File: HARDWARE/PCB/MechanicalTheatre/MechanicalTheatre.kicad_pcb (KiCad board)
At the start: 2 copper layers, 142.5 x 185 mm, 171 parts, among them J1 Power In 5V/24V, J10 Conn_01x02_General Purpose 01, J11 RJ45 8x Socket, J12 RJ45 8x Socket, J13 Conn_01x02_General Purpose 05, J14 Conn_01x02_General Purpose 06, J15 Conn_01x02_General Purpose 07, J16 Conn_01x02_General Purpose 10, J17 Conn_01x02_General Purpose 09, J18 Conn_01x02_General Purpose 08, J19 Conn_01x02_General Purpose 11, J2 Conn_01x02_General Purpose 02, J20 Conn_01x02_General Purpose 12, J21 Conn_01x02_General Purpose 13, J22 Conn_01x02_General Purpose 14, J23 Conn_01x02_General Purpose 03, J3 Conn_01x02_General Purpose 04, J4 Conn_01x06_Relais, J5 PQG3FST112, J6 Conn_01x03_ExternalSensor, J8 Conn_01x04_I2C_Display_20x4, J9 Conn_01x03_ProximitySensor, U1 Teensy4.1_OuterPins, U10 SN74HC14S, U11 SN74AHCT125N, U12 SN74AHCT125N, U13 SN74AHCT125N, U14 SN74HC14S, U15 Teensy4.1_OuterPins, U16 LM1117-3.3, U2 ESP32-DEVKITC-32D, U3 SN74AHCT125N, U4 SN74AHCT125N, U5 SN74AHCT125N, U6 SN74HC14S, U7 SN74AHCT125N, U8 SN74AHCT125N, U9 SN74AHCT125N

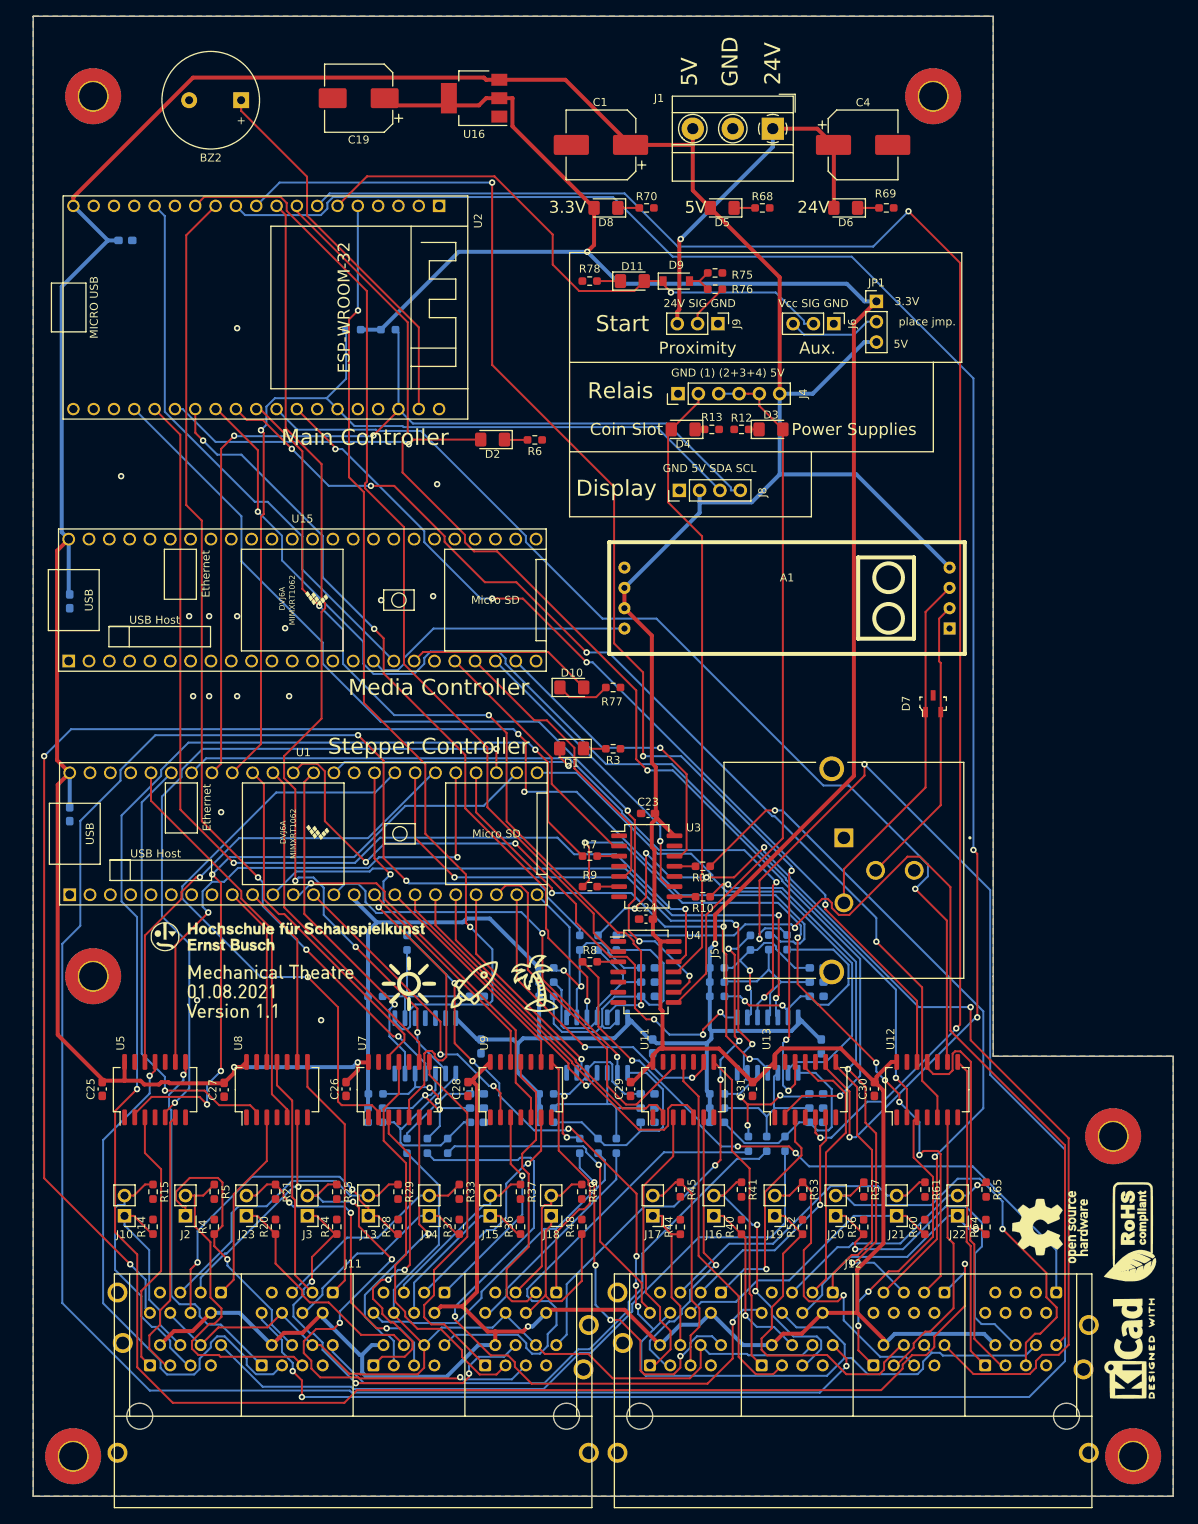
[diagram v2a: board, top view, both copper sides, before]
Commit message: pcb v1.2
- pcb v1.2 in production.
- startet to write a manual
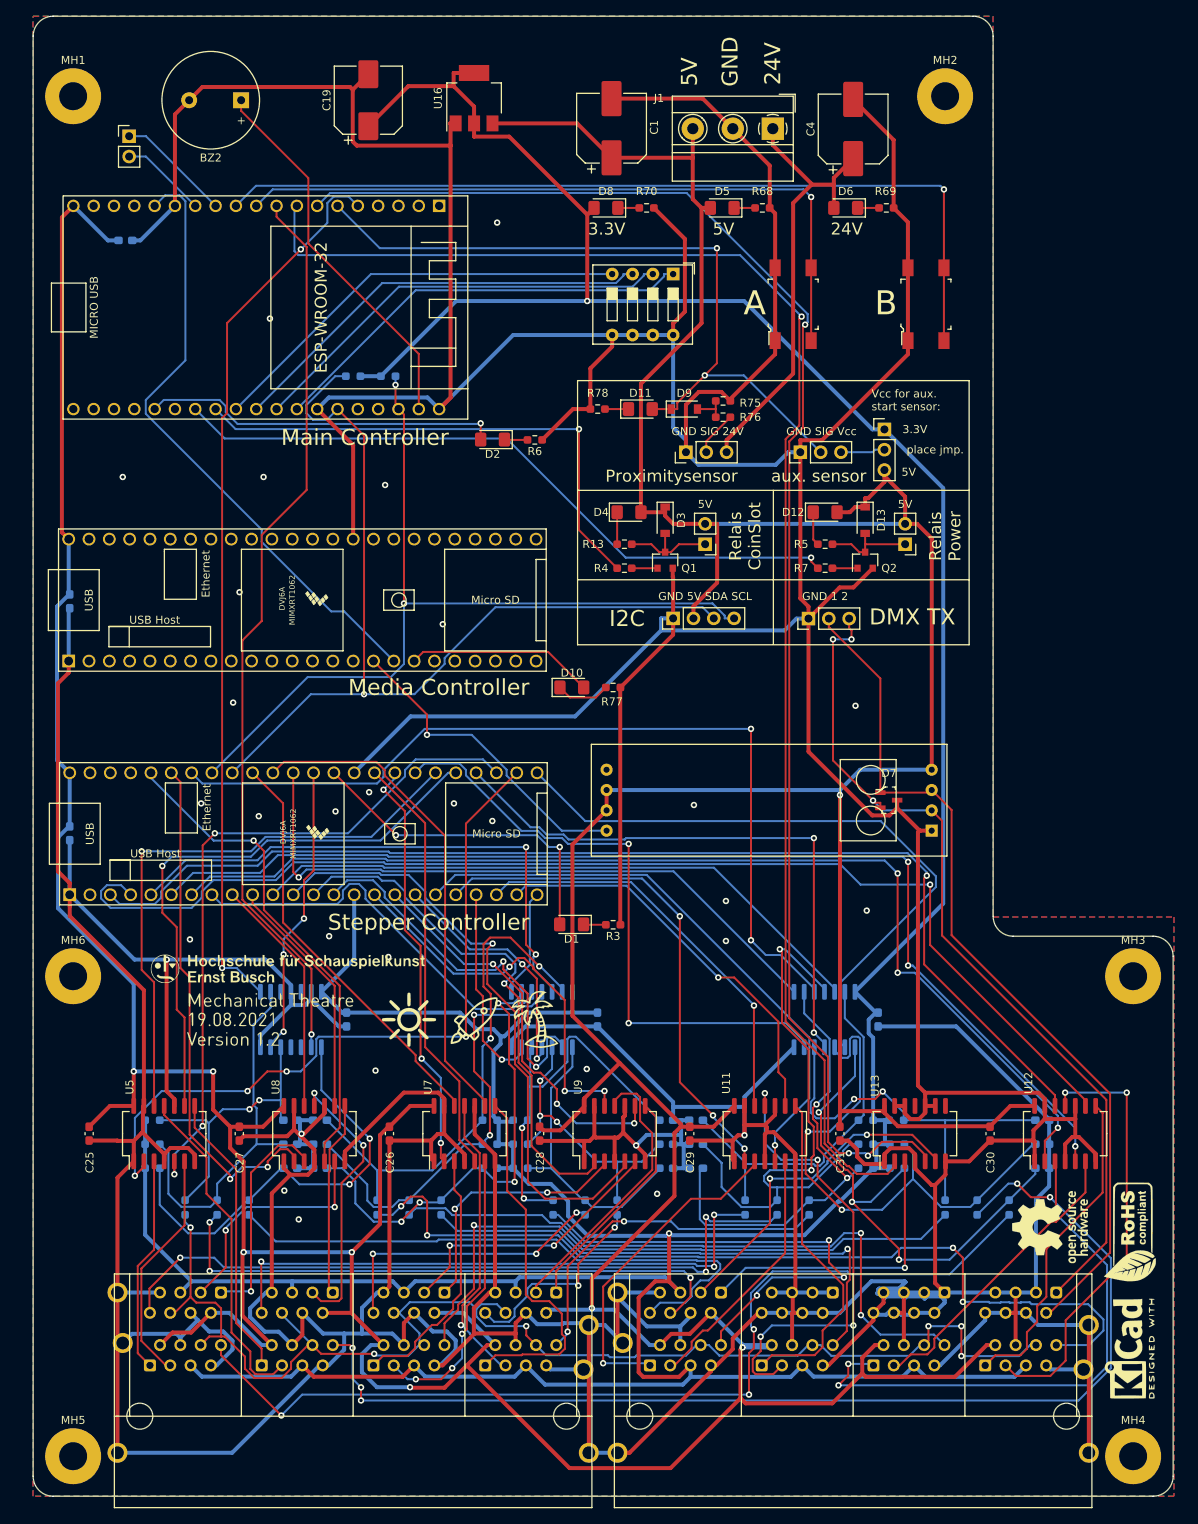
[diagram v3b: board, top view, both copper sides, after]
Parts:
- removed C20, C23, C24: 0.1uF 16V, Capacitor_SMD:C_0603_1608Metric_Pad1.08x0.95mm_HandSolder
- removed J10: Conn_01x02_General Purpose 01, Connector_PinHeader_2.54mm:PinHeader_1x02_P2.54mm_Vertical
- removed J13: Conn_01x02_General Purpose 05, Connector_PinHeader_2.54mm:PinHeader_1x02_P2.54mm_Vertical
- removed J14: Conn_01x02_General Purpose 06, Connector_PinHeader_2.54mm:PinHeader_1x02_P2.54mm_Vertical
- removed J15: Conn_01x02_General Purpose 07, Connector_PinHeader_2.54mm:PinHeader_1x02_P2.54mm_Vertical
- removed J16: Conn_01x02_General Purpose 10, Connector_PinHeader_2.54mm:PinHeader_1x02_P2.54mm_Vertical
- removed J17: Conn_01x02_General Purpose 09, Connector_PinHeader_2.54mm:PinHeader_1x02_P2.54mm_Vertical
- removed J18: Conn_01x02_General Purpose 08, Connector_PinHeader_2.54mm:PinHeader_1x02_P2.54mm_Vertical
- removed J19: Conn_01x02_General Purpose 11, Connector_PinHeader_2.54mm:PinHeader_1x02_P2.54mm_Vertical
- removed J20: Conn_01x02_General Purpose 12, Connector_PinHeader_2.54mm:PinHeader_1x02_P2.54mm_Vertical
- removed J21: Conn_01x02_General Purpose 13, Connector_PinHeader_2.54mm:PinHeader_1x02_P2.54mm_Vertical
- removed J22: Conn_01x02_General Purpose 14, Connector_PinHeader_2.54mm:PinHeader_1x02_P2.54mm_Vertical
- removed J23: Conn_01x02_General Purpose 03, Connector_PinHeader_2.54mm:PinHeader_1x02_P2.54mm_Vertical
- removed R10, R11, R12, R8, R9: 100, Resistor_SMD:R_0603_1608Metric_Pad0.98x0.95mm_HandSolder
- removed R14, R15, R20, R21, R24, R25, R28, R29, R32, R33, R36, R37, R40, R41, R44, R45, R48, R49, R52, R53, R56, R57, R60, R61, R64, R65, R66: 10k, Resistor_SMD:R_0603_1608Metric_Pad0.98x0.95mm_HandSolder
- removed R67: 1k, Resistor_SMD:R_0603_1608Metric_Pad0.98x0.95mm_HandSolder
- removed U3, U4: SN74AHCT125N, Package_SO:SO-14_5.3x10.2mm_P1.27mm
- removed mh1, mh2, mh3, mh4, mh5, mh6: MountingHole_3.5mm_Pad_TopBottom, MountingHole:MountingHole_3.5mm_Pad_TopBottom
- added D12: LED, LED_SMD:LED_1206_3216Metric_Pad1.42x1.75mm_HandSolder, F.Cu at (129.0, 102.0)
- added D13: 1N4148, Diode_SMD:D_SOD-123, F.Cu at (134.0, 103.0)
- added MH1: MountingHole_3.5mm_Pad, MountingHole:MountingHole_3.5mm_Pad, F.Cu at (35.0, 50.0)
- added MH2: MountingHole_3.5mm_Pad, MountingHole:MountingHole_3.5mm_Pad, F.Cu at (144.0, 50.0)
- added MH3: MountingHole_3.5mm_Pad, MountingHole:MountingHole_3.5mm_Pad, F.Cu at (167.5, 160.0)
- added MH4: MountingHole_3.5mm_Pad, MountingHole:MountingHole_3.5mm_Pad, F.Cu at (167.5, 220.0)
- added MH5: MountingHole_3.5mm_Pad, MountingHole:MountingHole_3.5mm_Pad, F.Cu at (35.0, 220.0)
- added MH6: MountingHole_3.5mm_Pad, MountingHole:MountingHole_3.5mm_Pad, F.Cu at (35.0, 160.0)
- added Q1: BC848, Package_TO_SOT_SMD:SOT-23, F.Cu at (109.0, 108.0)
- added Q2: BC848, Package_TO_SOT_SMD:SOT-23, F.Cu at (134.0, 108.0)
- added S1: Start Show, digikey-footprints:Switch_Tactile_SMD_6x6mm, F.Cu at (125.0, 76.0)
- added S2: Stop Show, digikey-footprints:Switch_Tactile_SMD_6x6mm, F.Cu at (141.6, 76.0)
- added SW1: SW_DIP_x04, Button_Switch_THT:SW_DIP_SPSTx04_Slide_9.78x12.34mm_W7.62mm_P2.54mm, F.Cu at (110.0, 72.2)
- D3: value LED -> 1N4148; footprint LED_SMD:LED_1206_3216Metric_Pad1.42x1.75mm_HandSolder -> Diode_SMD:D_SOD-123
- J2: value Conn_01x02_General Purpose 02 -> Conn_01x02_Male_Telefon?
- J3: value Conn_01x02_General Purpose 04 -> Conn_E-Magnet
- J4: value Conn_01x06_Relais -> Conn_PowerRelais; footprint Connector_PinHeader_2.54mm:PinHeader_1x06_P2.54mm_Vertical -> Connector_PinHeader_2.54mm:PinHeader_1x02_P2.54mm_Vertical
- J5: value PQG3FST112 -> Conn_01x03_Male_DMX_TX; footprint PQG3FST112:SWITCHCRAFT_PQG3FST112 -> Connector_PinHeader_2.54mm:PinHeader_1x03_P2.54mm_Vertical
- R4: value 10k -> 1k
- R5: value 10k -> 100
- R7: value 100 -> 1k
- moved J2 135.1 mm to (42.0, 55.0), turned to 0 degrees
- moved R5 111.3 mm to (129.0, 106.0), turned to 180 degrees
- moved J3 97.6 mm to (114.0, 106.0)
- moved R4 97.0 mm to (103.9, 109.0), turned to 180 degrees
- moved C12 48.0 mm to (65.9, 184.0), turned to 180 degrees
- moved R7 46.5 mm to (129.0, 109.0), turned to 180 degrees
- moved C15 45.7 mm to (65.9, 181.0), turned to 180 degrees
- moved R59 44.6 mm to (73.0, 188.9), turned to 90 degrees
- moved C16 43.8 mm to (65.9, 178.0), turned to 180 degrees
- moved R72 40.7 mm to (53.0, 188.9), turned to 270 degrees
- moved R55 40.7 mm to (77.0, 188.9), turned to 90 degrees
- moved R43 37.4 mm to (81.0, 188.9), turned to 90 degrees
- moved J4 34.1 mm to (139.0, 106.0), turned to 180 degrees
- moved R27 33.9 mm to (127.0, 188.9), turned to 90 degrees
- moved R35 33.6 mm to (119.0, 188.9), turned to 90 degrees
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- renumbered G*** to G1
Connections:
- net /ESP_GENERAL_ENDSWITCH_DEBOUNCED renamed Net-(U14-Pad8)
- D3 pad 1: Net-(D3-Pad1) -> +5V
- D4 pad 2: Net-(D4-Pad2) -> +5V
- J11 pad 14: Net-(J10-Pad1) -> GND
- J11 pad 15: Net-(J10-Pad2) -> +3V3
- J11 pad 24: Net-(J11-Pad24) -> GND
- J11 pad 25: Net-(J11-Pad25) -> +3V3
- J11 pad 34: Net-(J11-Pad34) -> GND
- J11 pad 35: Net-(J11-Pad35) -> +3V3
- J11 pad 44: Net-(J11-Pad44) -> GND
- J11 pad 45: Net-(J11-Pad45) -> +3V3
- J11 pad 54: Net-(J11-Pad54) -> GND
- J11 pad 55: Net-(J11-Pad55) -> +3V3
- J11 pad 64: Net-(J11-Pad64) -> GND
- J11 pad 65: Net-(J11-Pad65) -> +3V3
- J11 pad 74: Net-(J11-Pad74) -> GND
- J11 pad 75: Net-(J11-Pad75) -> +3V3
- J11 pad 84: Net-(J11-Pad84) -> GND
- J11 pad 85: Net-(J11-Pad85) -> +3V3
- J12 pad 14: Net-(J12-Pad14) -> GND
- J12 pad 15: Net-(J12-Pad15) -> +3V3
- J12 pad 24: Net-(J12-Pad24) -> GND
- J12 pad 25: Net-(J12-Pad25) -> +3V3
- J12 pad 34: Net-(J12-Pad34) -> GND
- J12 pad 35: Net-(J12-Pad35) -> +3V3
- J12 pad 36: /GENERAL_END_SWITCH_ESP -> /GENERAL_END_SWITCH_TEENSY
- J12 pad 44: Net-(J12-Pad44) -> GND
- J12 pad 45: Net-(J12-Pad45) -> +3V3
- J12 pad 46: /GENERAL_END_SWITCH_ESP -> /GENERAL_END_SWITCH_TEENSY
- J12 pad 54: Net-(J12-Pad54) -> GND
- J12 pad 55: Net-(J12-Pad55) -> +3V3
- J12 pad 56: /GENERAL_END_SWITCH_ESP -> /Stepper Connection 13/END_ALL
- J12 pad 61: Net-(J12-Pad61) -> GND
- J12 pad 62: +5V -> GND
- J12 pad 63: Net-(J12-Pad63) -> GND
- J12 pad 64: Net-(J12-Pad64) -> GND
- J12 pad 65: Net-(J12-Pad65) -> GND
- J12 pad 66: /GENERAL_END_SWITCH_ESP -> GND
- J12 pad 68: Net-(J12-Pad68) -> GND
- J12 pad 71: Net-(J12-Pad71) -> GND
- J12 pad 73: Net-(J12-Pad73) -> GND
- J12 pad 75: Net-(J12-Pad75) -> GND
- J12 pad 77: Net-(J12-Pad77) -> GND
- J12 pad 81: Net-(J12-Pad81) -> Net-(A1-Pad3)
- J12 pad 82: GND -> Net-(A1-Pad2)
- J2 pad 1: Net-(J11-Pad24) -> Net-(J2-Pad1)
- J2 pad 2: Net-(J11-Pad25) -> Net-(J2-Pad2)
- J3 pad 1: Net-(J11-Pad44) -> Net-(D3-Pad2)
- J3 pad 2: Net-(J11-Pad45) -> +5V
- J4 pad 1: GND -> Net-(D13-Pad2)
- J4 pad 2: Net-(D4-Pad2) -> +5V
- R13 pad 1: GND -> Net-(D3-Pad2)
- R4 pad 1: Net-(J11-Pad24) -> Net-(Q1-Pad1)
- R4 pad 2: GND -> /RELAIS_E-MAGNET
- R5 pad 1: Net-(J11-Pad25) -> Net-(D13-Pad2)
- R5 pad 2: GND -> Net-(D12-Pad1)
- R7 pad 1: Net-(J12-Pad71) -> Net-(Q2-Pad1)
- R7 pad 2: Net-(R7-Pad2) -> /RELAIS_24V+5V
- R72 pad 2: /GENERAL_END_SWITCH_ESP -> /Stepper Connection 13/END_ALL
- U1 pad 3: Net-(U1-Pad3) -> /STEPPER_12_STEP
- U1 pad 4: Net-(U1-Pad4) -> /STEPPER_12_DIR
- U1 pad 5: Net-(U1-Pad5) -> /STEPPER_12_END
- U1 pad 6: Net-(U1-Pad6) -> /STEPPER_11_STEP
- U1 pad 7: Net-(U1-Pad7) -> /STEPPER_11_DIR
- U1 pad 8: Net-(U1-Pad8) -> /STEPPER_11_END
- U13 pad 11: Net-(J12-Pad63) -> Net-(U13-Pad11)
- U13 pad 12: /STEPPER_14_STEP -> GND
- U13 pad 8: Net-(J12-Pad61) -> Net-(U13-Pad8)
- U13 pad 9: /STEPPER_14_DIR -> GND
- U14 pad 10: (no net) -> Net-(U14-Pad10)
- U14 pad 11: (no net) -> GND
- U14 pad 12: (no net) -> Net-(U14-Pad12)
- U14 pad 13: (no net) -> GND
- U14 pad 3: Net-(C20-Pad1) -> (no net)
- U14 pad 4: /STEPPER_14_END -> (no net)
- U15 pad 20: /WS2812B_Line_1 -> Net-(U15-Pad20)
- U15 pad 21: /WS2812B_Line_2 -> Net-(U15-Pad21)
- U15 pad 22: /WS2812B_Line_3 -> Net-(U15-Pad22)
- U15 pad 23: /WS2812B_Line_4 -> Net-(U15-Pad23)
- U2 pad 10: /STEPPER_14_STEP -> Net-(S1-Pad3)
- U2 pad 11: /STEPPER_14_DIR -> Net-(S2-Pad3)
- U2 pad 12: /STEPPER_14_END -> Net-(J2-Pad1)
- U2 pad 13: /WS2812B_LED_LIGHTING -> Net-(J2-Pad2)
- U2 pad 27: /STEPPER_12_STEP -> Net-(SW1-Pad1)
- U2 pad 28: /STEPPER_12_DIR -> Net-(SW1-Pad2)
- U2 pad 29: /STEPPER_12_END -> Net-(SW1-Pad3)
- U2 pad 30: /STEPPER_11_STEP -> Net-(SW1-Pad4)
- U2 pad 31: /STEPPER_11_DIR -> /RELAIS_E-MAGNET
- U2 pad 32: /STEPPER_11_END -> /RELAIS_24V+5V
- U2 pad 33: Net-(D2-Pad2) -> Net-(U2-Pad33)
- U2 pad 34: /RELAIS_E-MAGNET -> Net-(D2-Pad2)
- U2 pad 35: /RELAIS_24V+5V -> Net-(U2-Pad35)
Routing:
- net GND: track 0.00 -> 1586.1 mm, vias 16 -> 31
- net Net-(J12-Pad71): track 265.4 -> 0.00 mm, vias 3 -> 0
- net +3V3: track 348.6 -> 603.3 mm
- net /STEPPER_14_DIR: track 216.3 -> 0.00 mm, vias 3 -> 0
- net Net-(J12-Pad28): track 254.5 -> 66.1 mm, vias 3 -> 1
- net /STEPPER_14_STEP: track 167.2 -> 0.00 mm, vias 5 -> 0
- net Net-(J11-Pad68): track 226.8 -> 73.7 mm, vias 4 -> 3
- net /GENERAL_END_SWITCH_ESP: track 140.5 -> 0.00 mm, vias 6 -> 0
- net /WS2812B_LED_LIGHTING: track 123.6 -> 0.00 mm
- net /STEPPER_14_END: track 122.7 -> 0.00 mm, vias 3 -> 0
- net +5V: track 690.2 -> 810.7 mm, vias 3 -> 8
- net Net-(S2-Pad3): track 0.00 -> 108.6 mm, vias 0 -> 1
- net Net-(J11-Pad58): track 192.5 -> 91.2 mm, vias 4 -> 3
- net Net-(J12-Pad73): track 93.7 -> 0.00 mm, vias 6 -> 0
- net Net-(S1-Pad3): track 0.00 -> 88.6 mm, vias 0 -> 1
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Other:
- outline, holes or cut-outs redrawn
- board text added: "A"
- board text added: "B"
- board text added: "DMX TX"
- board text added: "GND 1 2"
- board text added: "GND SIG 24V"
- board text added: "GND SIG Vcc"
- board text added: "I2C"
- board text added: "Proximitysensor"
- board text added: "Relais CoinSlot"
- board text added: "Relais Power"
- board text added: "Vcc for aux. start sensor:"
- board text added: "aux. sensor"
- board text removed: "24V SIG GND"
- board text removed: "Aux."
- board text removed: "Coin Slot"
- board text removed: "Display"
- board text removed: "GND (1) (2+3+4) 5V"
- board text removed: "Power Supplies"
- board text removed: "Proximity"
- board text removed: "Relais"
- board text removed: "Start"
- board text removed: "Vcc SIG GND"
